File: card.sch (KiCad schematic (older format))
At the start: 0 parts

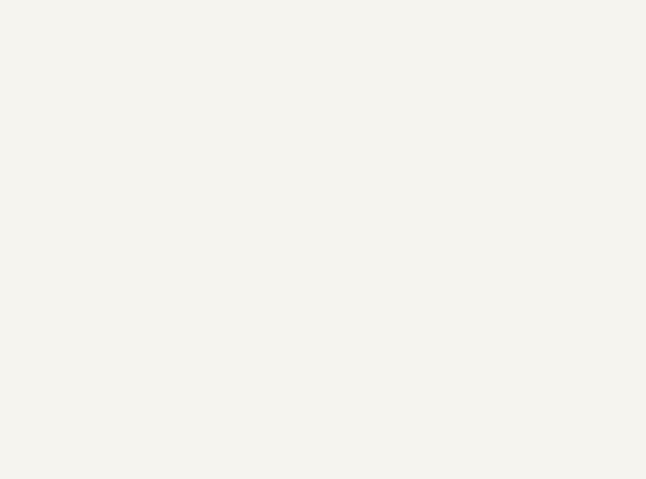
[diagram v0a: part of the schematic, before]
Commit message: added sheeT for CPU
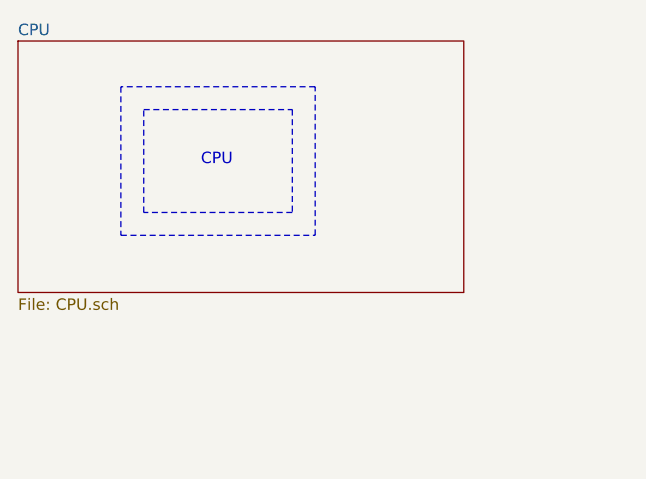
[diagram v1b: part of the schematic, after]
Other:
- note added: "CPU\n"
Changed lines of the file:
@@
 $Descr A4 11693 8268
 encoding utf-8
-Sheet 1 2
+Sheet 1 3
 Title ""
 Date ""
@@
 F1 "power.sch" 50
 $EndSheet
+$Sheet
+S 850  800  1950 1100
+U 5F4BE60C
+F0 "CPU" 50
+F1 "CPU.sch" 50
+$EndSheet
+Wire Notes Line
+	1300 1000 1300 1650
+Wire Notes Line
+	1300 1650 2150 1650
+Wire Notes Line
+	2150 1650 2150 1000
+Wire Notes Line
+	2150 1000 1300 1000
+Wire Notes Line
+	1400 1100 2050 1100
+Wire Notes Line
+	2050 1100 2050 1550
+Wire Notes Line
+	2050 1550 1400 1550
+Wire Notes Line
+	1400 1550 1400 1100
+Text Notes 1650 1350 0    50   ~ 0
+CPU\n
 $EndSCHEMATC

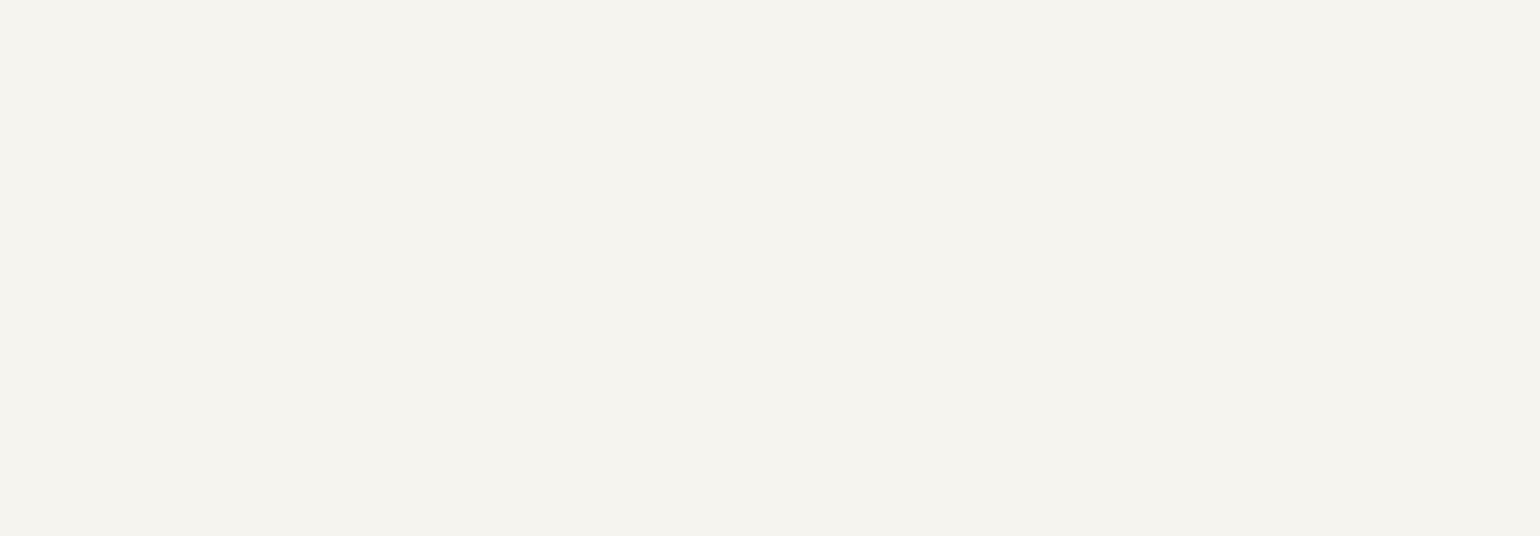
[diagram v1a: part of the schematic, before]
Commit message: added port / GPIO sheet to scimatic
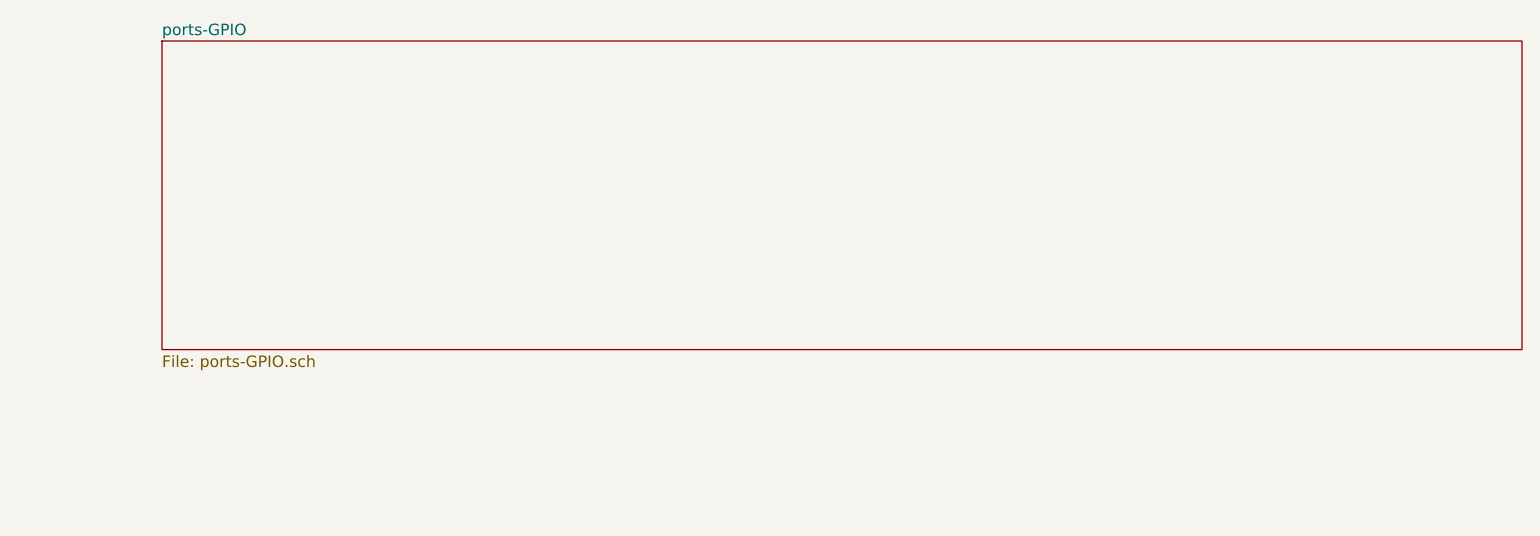
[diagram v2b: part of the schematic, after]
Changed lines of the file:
@@
 $Descr A4 11693 8268
 encoding utf-8
-Sheet 1 3
+Sheet 1 4
 Title ""
 Date ""
@@
 Text Notes 1650 1350 0    50   ~ 0
 CPU\n
+$Sheet
+S 3800 800  5950 1350
+U 5F529CC2
+F0 "ports-GPIO" 50
+F1 "ports-GPIO.sch" 50
+$EndSheet
 $EndSCHEMATC

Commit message: added todo list before i feel aleeped on my keybard*
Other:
- note added: "PSU"
- note added: "TO DO :\n - add blue bean modlue \n - add footprints for all compontents\n - add symble for MOSFET"
- note added: "TO DO :\n - add symbol for MOSFET\n - add footprint and symble for blue bean module\n - add asign footprints for all components\n - check avalability of parts for power suply"
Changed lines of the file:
@@
 $EndDescr
 $Sheet
-S 3800 4250 2200 1300
+S 850  6250 2200 1300
 U 5F46881F
 F0 "Power" 50
@@
 F1 "ports-GPIO.sch" 50
 $EndSheet
+Text Notes 5600 3350 0    0    ~ 0
+TO DO :\n - add blue bean modlue \n - add footprints for all compontents\n - add symble for MOSFET
+Text Notes 2750 3800 0    197  ~ 0
+TO DO  :\n - add symbol for MOSFET\n - add footprint and symble for blue bean module\n - add asign footprints for all components\n - check avalability of parts for power suply
+Wire Notes Line
+	1150 6550 1150 7300
+Wire Notes Line
+	1150 7300 2700 7300
+Wire Notes Line
+	2700 7300 2700 6550
+Wire Notes Line
+	2700 6550 1150 6550
+Wire Notes Line
+	2200 6700 2200 7050
+Wire Notes Line
+	2200 7050 2250 7050
+Wire Notes Line
+	2250 7050 2250 6700
+Wire Notes Line
+	2250 6700 2200 6700
+Wire Notes Line
+	2300 6700 2300 7050
+Wire Notes Line
+	2300 7050 2350 7050
+Wire Notes Line
+	2350 7050 2350 6700
+Wire Notes Line
+	2350 6700 2300 6700
+Wire Notes Line
+	2400 6700 2400 7050
+Wire Notes Line
+	2400 7050 2450 7050
+Wire Notes Line
+	2450 7050 2450 6700
+Wire Notes Line
+	2450 6700 2400 6700
+Text Notes 1300 6750 0    79   ~ 0
+PSU
 $EndSCHEMATC

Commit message: finished scimatic for now, and started populating PCB. *chugs rrum*
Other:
- note added: "TO DO :\n - check footprint for components. \n - crycstal\n - power stuff\n - CPU\n - check avalability of parts for power suply\n - find crystal, and psu parts on digikey\n"
- note removed: "TO DO :\n - add symbol for MOSFET\n - add footprint and symble for blue bean module\n - add asign footprints for all components\n - check avalability of parts for power suply"
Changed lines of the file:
@@
 $Descr A4 11693 8268
 encoding utf-8
-Sheet 1 4
+Sheet 1 5
 Title ""
 Date ""
@@
 Text Notes 5600 3350 0    0    ~ 0
 TO DO :\n - add blue bean modlue \n - add footprints for all compontents\n - add symble for MOSFET
-Text Notes 2750 3800 0    197  ~ 0
-TO DO  :\n - add symbol for MOSFET\n - add footprint and symble for blue bean module\n - add asign footprints for all components\n - check avalability of parts for power suply
+Text Notes 2650 4400 0    197  ~ 0
+TO DO  :\n - check footprint for components. \n  - crycstal\n  - power stuff\n  - CPU\n - check avalability of parts for power suply\n - find crystal, and psu parts on digikey\n
 Wire Notes Line
 	1150 6550 1150 7300
@@
 Text Notes 1300 6750 0    79   ~ 0
 PSU
+$Sheet
+S 4300 4750 850  1000
+U 5F56A00E
+F0 "BlueBean" 50
+F1 "BlueBean.sch" 50
+$EndSheet
 $EndSCHEMATC
